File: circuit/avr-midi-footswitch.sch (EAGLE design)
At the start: 28 parts, among them IC1 MEGA328P, IC2 7805, Q1 8M

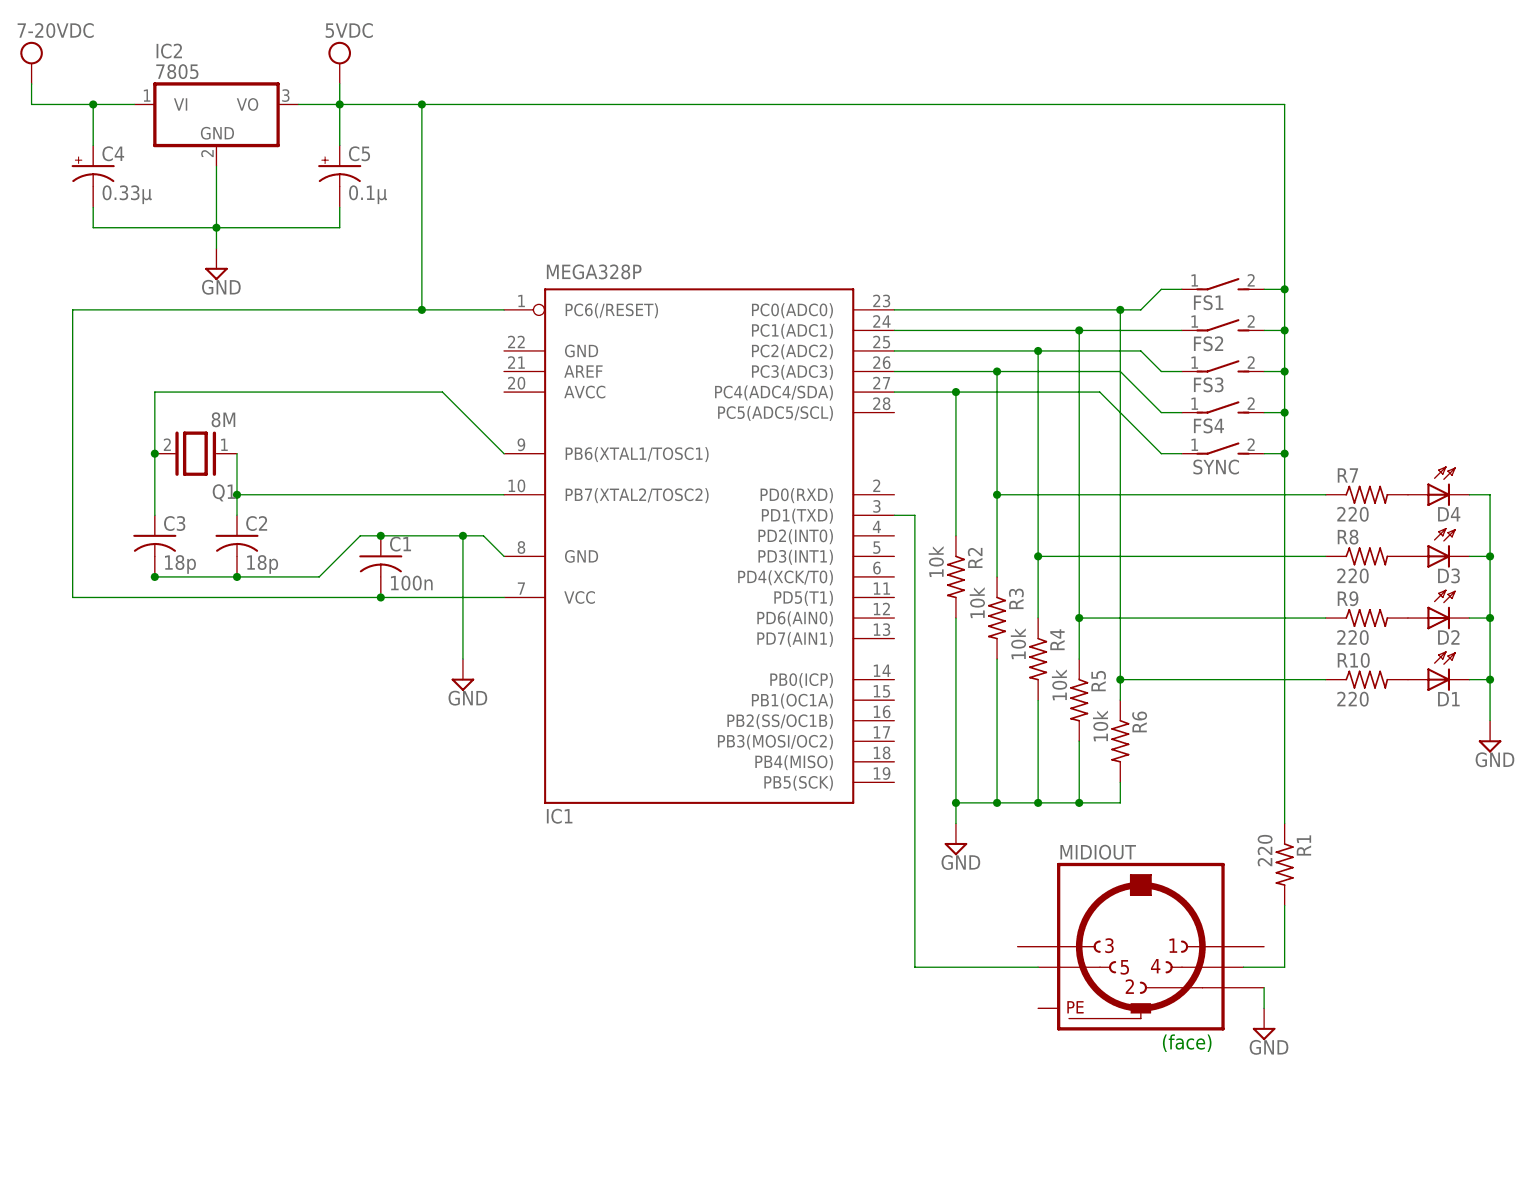
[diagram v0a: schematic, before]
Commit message: A major update
In this update:

* Add support for momentary switches and MCU-controlled LEDs.

* Add optional power-up time LED animation.

* Refactor whole project so that footswitches are even more
  independently configured (see changes in `README.md` for more
  details).

* Make UART configurable with definitions in `config.h`.

* Use `const` thoroughly.

* Add comments.

Signed-off-by: Philippe Proulx <eeppeliteloop@gmail.com>
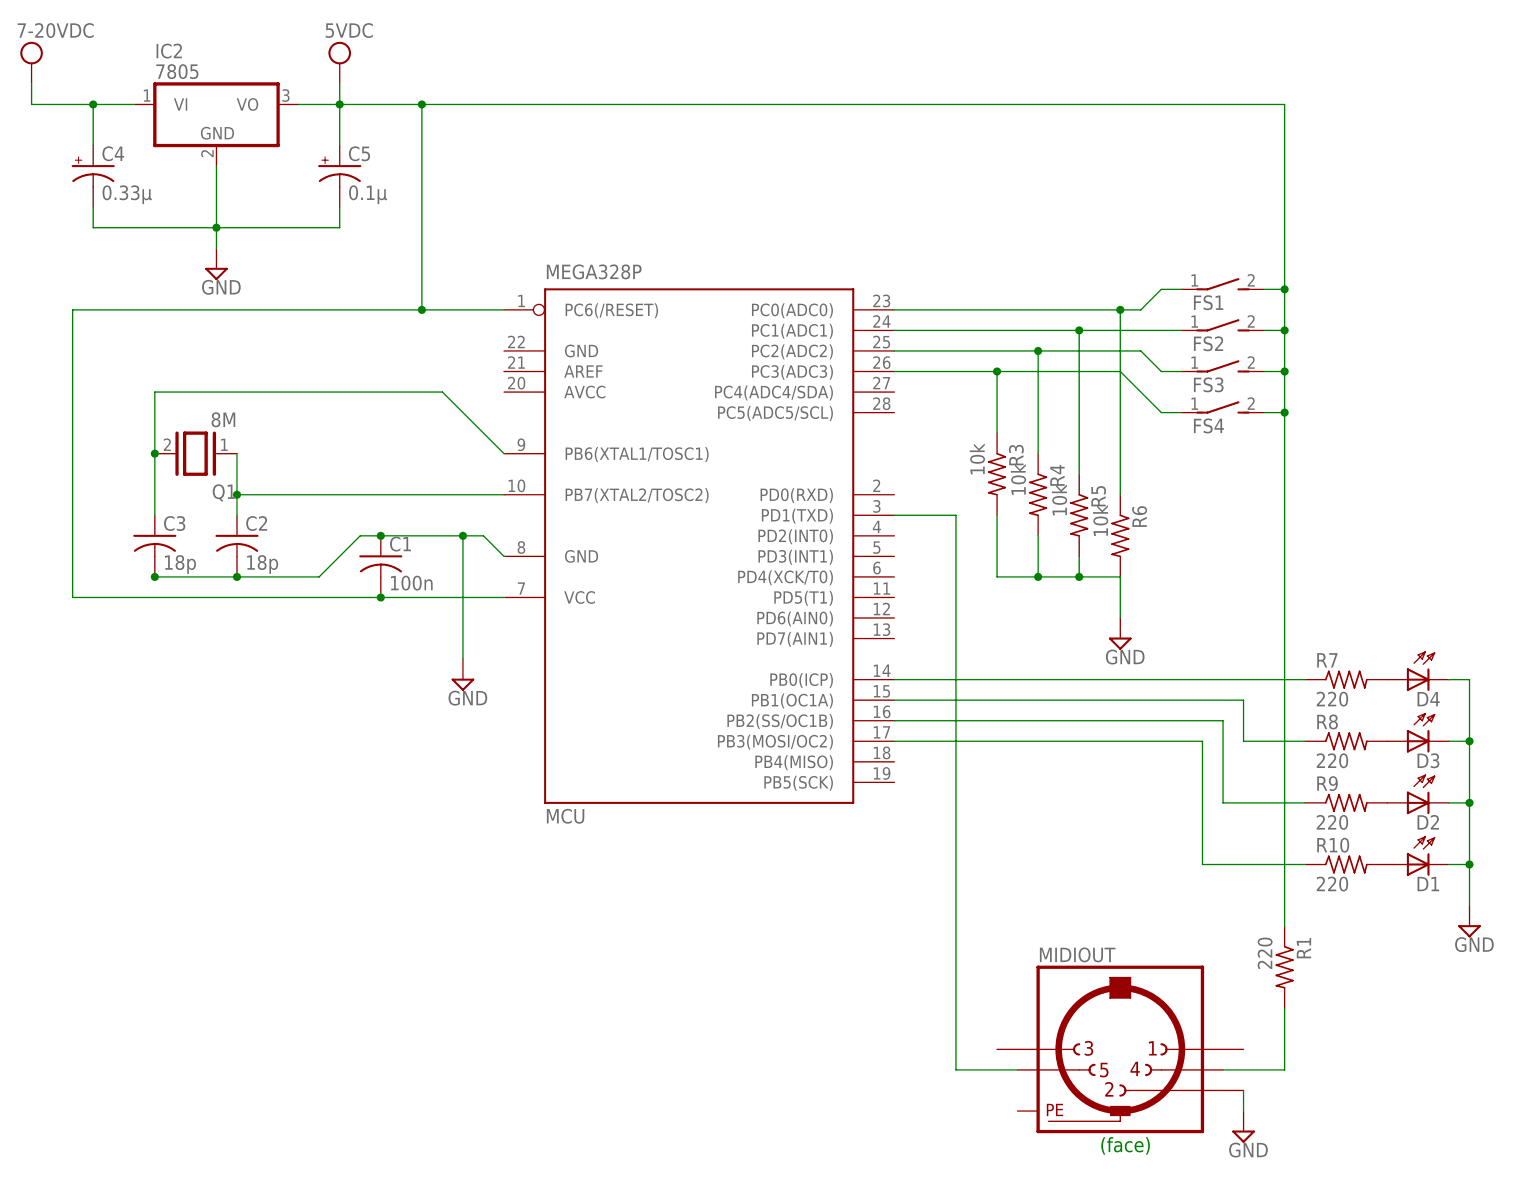
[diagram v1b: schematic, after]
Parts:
- removed R2: 10k, resistor:R-US_0204/2V
- removed SYNC: (no value), switch-dil:DS01E
- renumbered IC1 to MCU
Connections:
- new net N$15: MCU.PB2(SS/OC1B), R9.1
- new net N$16: MCU.PB3(MOSI/OC2), R10.1
- new net N$7: MCU.PB0(ICP), R7.1
- net GND: no longer R2.2
- net N$10: now also MCU.PB1(OC1A), R8.1; no longer MCU.PC4(ADC4/SDA), R2.1, SYNC.1
- net N$5: no longer R10.1
- net N$6: no longer R9.1
- net N$8: no longer R8.1
- net N$9: no longer R7.1
- net VCC: no longer SYNC.2
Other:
- moved on the sheet: D1, D2, D3, D4, MIDIOUT, R1, R10, R3, R4, R5, R6, R7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
